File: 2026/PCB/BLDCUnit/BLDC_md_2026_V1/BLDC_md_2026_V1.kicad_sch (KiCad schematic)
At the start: 65 parts, among them J1 Conn_01x07_Pin, J2 Conn_01x02_Pin, J3 Conn_01x03_Socket, J4 Conn_01x02_Socket, J5 Conn_01x06_Socket, SW1 SW_MEC_5E, SW2 SW_MEC_5E, U1 MAX3051

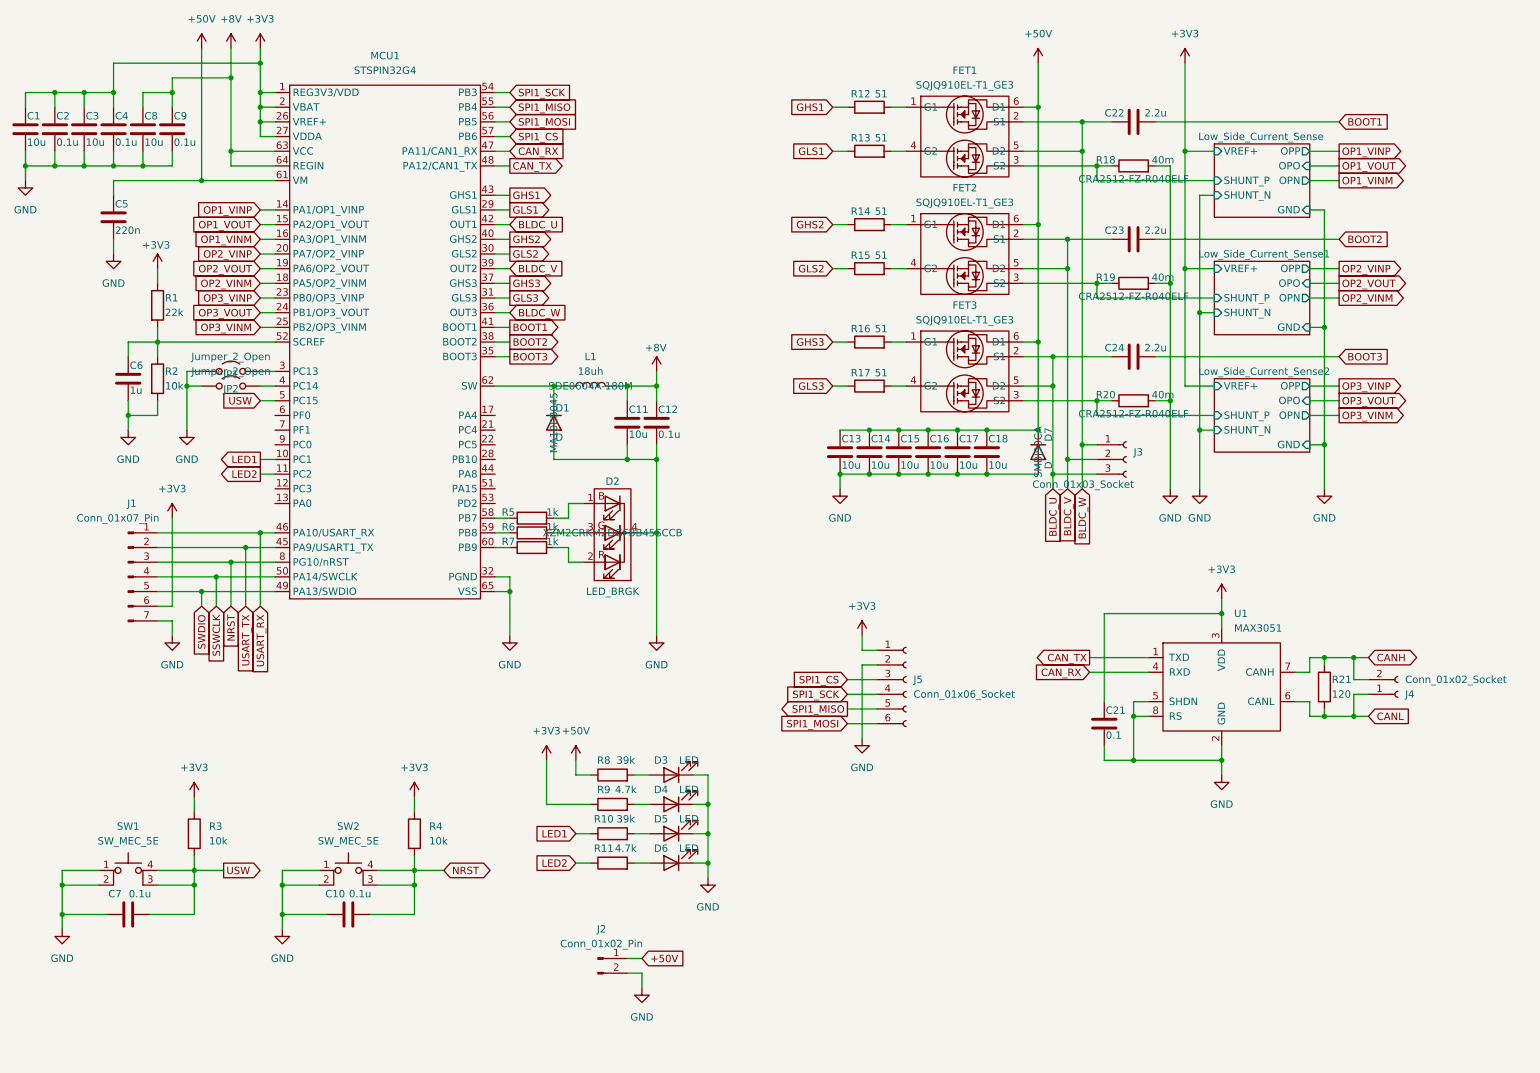
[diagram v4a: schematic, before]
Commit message: 外形縮小＆モエチャッカファイヤ回避
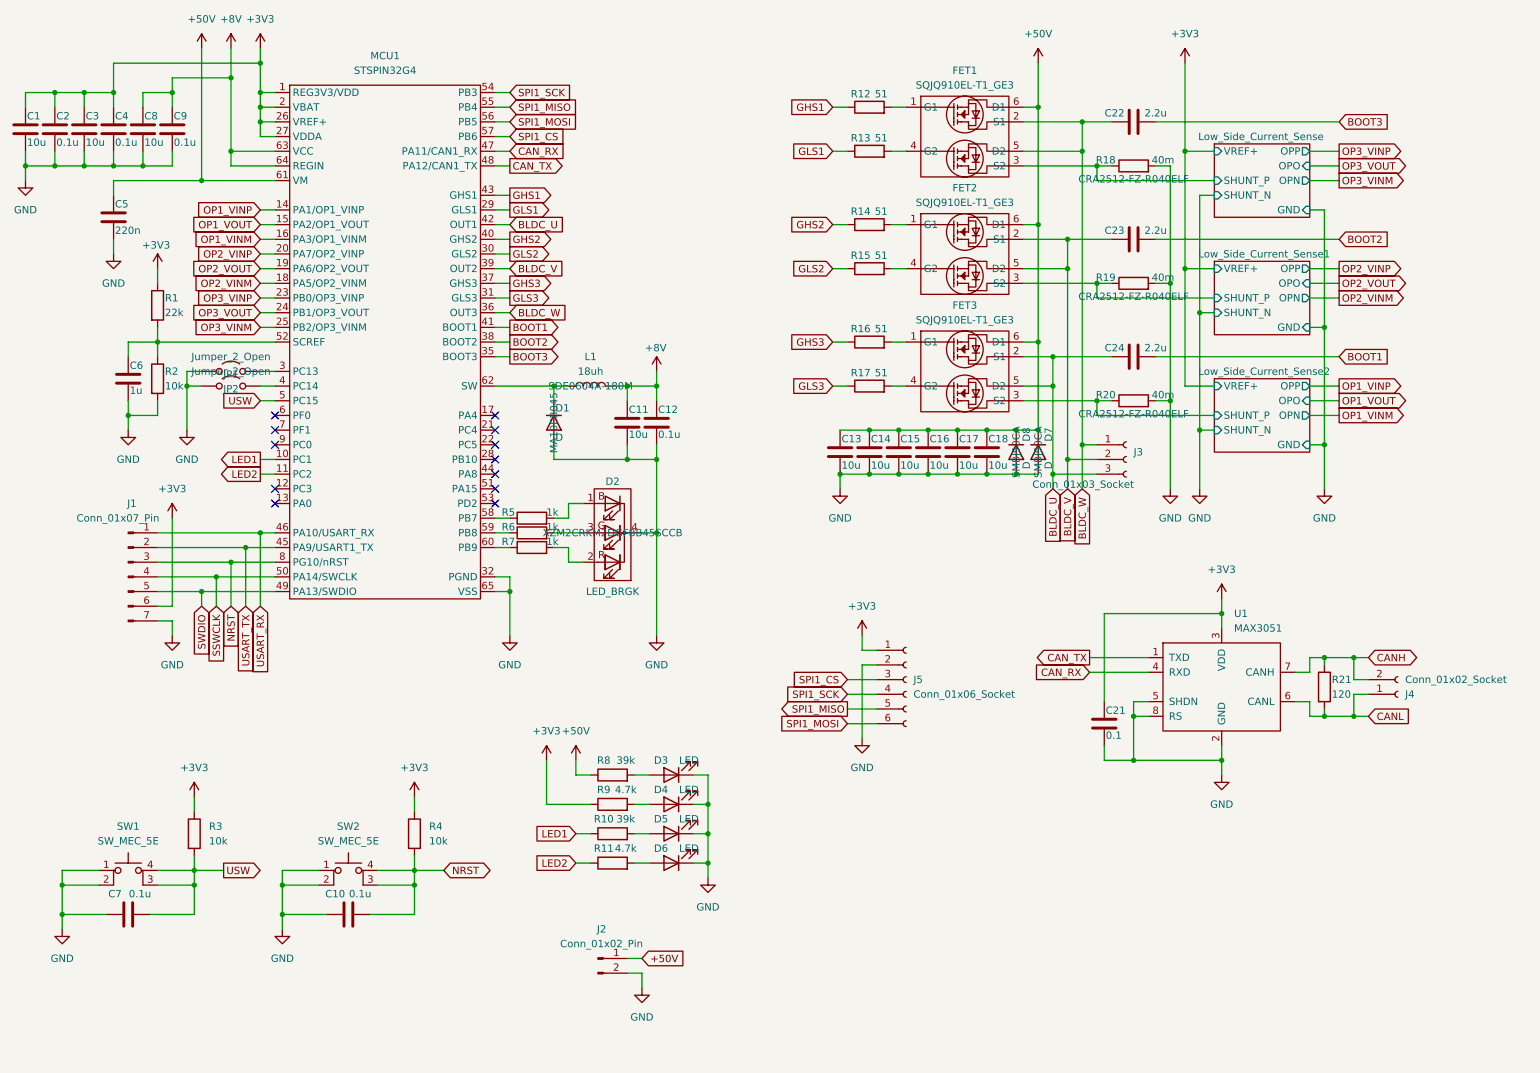
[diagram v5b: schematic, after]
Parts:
- added D8: D, Diode_SMD:D_SMB, symbol Device:D
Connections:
- net +50V: now also D8.1 (K)
- net BOOT1: now also C24.2; no longer C22.2
- net BOOT3: now also C22.2; no longer C24.2
- net GND: now also D8.2 (A)
- no-connect marks 0 -> 12
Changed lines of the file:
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@@
 	)
 	(junction
+		(at 194.31 87.63)
+		(diameter 0)
+		(color 0 0 0 0)
+	)
+	(junction
 		(at 229.87 119.38)
 		(diameter 0)
@@
 	)
 	(junction
+		(at 194.31 95.25)
+		(diameter 0)
+		(color 0 0 0 0)
+	)
+	(junction
 		(at 140.97 152.4)
 		(diameter 0)
@@
 		(color 0 0 0 0)
 	)
+	(no_connect
+		(at 104.14 92.71)
+	)
+	(no_connect
+		(at 66.04 87.63)
+	)
+	(no_connect
+		(at 66.04 100.33)
+	)
+	(no_connect
+		(at 104.14 97.79)
+	)
+	(no_connect
+		(at 104.14 100.33)
+	)
+	(no_connect
+		(at 104.14 87.63)
+	)
+	(no_connect
+		(at 66.04 90.17)
+	)
+	(no_connect
+		(at 104.14 90.17)
+	)
+	(no_connect
+		(at 104.14 85.09)
+	)
+	(no_connect
+		(at 104.14 95.25)
+	)
+	(no_connect
+		(at 66.04 97.79)
+	)
+	(no_connect
+		(at 66.04 85.09)
+	)
 	(wire
 		(pts
@@
 	(wire
 		(pts
-			(xy 189.23 95.25) (xy 198.12 95.25)
+			(xy 189.23 95.25) (xy 194.31 95.25)
 		)
 		(stroke
@@
 	(wire
 		(pts
-			(xy 189.23 87.63) (xy 198.12 87.63)
+			(xy 189.23 87.63) (xy 194.31 87.63)
 		)
 		(stroke
@@
 	(wire
 		(pts
+			(xy 194.31 95.25) (xy 198.12 95.25)
+		)
+		(stroke
+			(width 0)
+			(type default)
+		)
+	)
+	(wire
+		(pts
 			(xy 38.1 24.13) (xy 63.5 24.13)
 		)
@@
 	(wire
 		(pts
+			(xy 194.31 87.63) (xy 198.12 87.63)
+		)
+		(stroke
+			(width 0)
+			(type default)
+		)
+	)
+	(wire
+		(pts
 			(xy 140.97 157.48) (xy 140.97 162.56)
 		)
@@
 	(global_label "OP1_VINM"
 		(shape output)
-		(at 250.19 44.45 0)
+		(at 250.19 85.09 0)
 		(fields_autoplaced yes)
 		(effects
@@
 		)
 		(property "Intersheetrefs" "${INTERSHEET_REFS}"
-			(at 262.4281 44.45 0)
+			(at 262.4281 85.09 0)
 			(effects
 				(font
@@
 	(global_label "OP1_VINP"
 		(shape output)
-		(at 250.19 39.37 0)
+		(at 250.19 80.01 0)
 		(fields_autoplaced yes)
 		(effects
@@
 		)
 		(property "Intersheetrefs" "${INTERSHEET_REFS}"
-			(at 262.2467 39.37 0)
+			(at 262.2467 80.01 0)
 			(effects
 				(font
@@
 	(global_label "OP3_VINM"
 		(shape output)
-		(at 250.19 85.09 0)
+		(at 250.19 44.45 0)
 		(fields_autoplaced yes)
 		(effects
@@
 		)
 		(property "Intersheetrefs" "${INTERSHEET_REFS}"
-			(at 262.4281 85.09 0)
+			(at 262.4281 44.45 0)
 			(effects
 				(font
@@
 	(global_label "BOOT1"
 		(shape input)
-		(at 250.19 34.29 0)
+		(at 250.19 74.93 0)
 		(fields_autoplaced yes)
 		(effects
@@
 		)
 		(property "Intersheetrefs" "${INTERSHEET_REFS}"
-			(at 259.2833 34.29 0)
+			(at 259.2833 74.93 0)
 			(effects
 				(font
@@
 	(global_label "OP3_VOUT"
 		(shape output)
-		(at 250.19 82.55 0)
+		(at 250.19 41.91 0)
 		(fields_autoplaced yes)
 		(effects
@@
 		)
 		(property "Intersheetrefs" "${INTERSHEET_REFS}"
-			(at 262.67 82.55 0)
+			(at 262.67 41.91 0)
 			(effects
 				(font
@@
 	(global_label "OP3_VINP"
 		(shape output)
-		(at 250.19 80.01 0)
+		(at 250.19 39.37 0)
 		(fields_autoplaced yes)
 		(effects
@@
 		)
 		(property "Intersheetrefs" "${INTERSHEET_REFS}"
-			(at 262.2467 80.01 0)
+			(at 262.2467 39.37 0)
 			(effects
 				(font
@@
 	(global_label "BOOT3"
 		(shape input)
-		(at 250.19 74.93 0)
+		(at 250.19 34.29 0)
 		(fields_autoplaced yes)
 		(effects
@@
 		)
 		(property "Intersheetrefs" "${INTERSHEET_REFS}"
-			(at 259.2833 74.93 0)
+			(at 259.2833 34.29 0)
 			(effects
 				(font
@@
 	(global_label "OP1_VOUT"
 		(shape output)
-		(at 250.19 41.91 0)
+		(at 250.19 82.55 0)
 		(fields_autoplaced yes)
 		(effects
@@
 		)
 		(property "Intersheetrefs" "${INTERSHEET_REFS}"
-			(at 262.67 41.91 0)
+			(at 262.67 82.55 0)
 			(effects
 				(font
@@
 					(unit 1)
 				)
+			)
+		)
+	)
+	(symbol
+		(lib_id "Device:D")
+		(at 194.31 91.44 270)
+		(unit 1)
+		(exclude_from_sim no)
+		(in_bom yes)
+		(on_board yes)
+		(dnp no)
+		(property "Reference" "D8"
+			(at 196.088 88.392 0)
+			(effects
+				(font
+					(size 1.27 1.27)
+				)
+			)
+		)
+		(property "Value" "D"
+			(at 196.088 93.726 0)
+			(effects
+				(font
+					(size 1.27 1.27)
+				)
+			)
+		)
+		(property "Footprint" "Diode_SMD:D_SMB"
+			(at 194.31 91.44 0)
+			(effects
+				(font
+					(size 1.27 1.27)
+				)
+				(hide yes)
+			)
+		)
+		(property "Datasheet" "~"
+			(at 194.31 91.44 0)
+			(effects
+				(font
+					(size 1.27 1.27)
+				)
+				(hide yes)
+			)
+		)
+		(property "Description" "SMBJ90CA"
+			(at 194.31 91.44 0)
+			(effects
+				(font
+					(size 1.27 1.27)
+				)
+			)
+		)
+		(property "Sim.Device" "D"
+			(at 194.31 91.44 0)
+			(effects
+				(font
+					(size 1.27 1.27)
+				)
+				(hide yes)
+			)
+		)
+		(property "Sim.Pins" "1=K 2=A"
+			(at 194.31 91.44 0)
+			(effects
+				(font
+					(size 1.27 1.27)
+				)
+				(hide yes)
+			)
+		)
+		(pin "1"
+		)
+		(pin "2"
+		)
+		(instances
+			(project "BLDC_md_2026_V1"
+				(path "/b60d34e1-e978-4abb-befd-6af7b603dc53"
+					(reference "D8")
+					(unit 1)
+				)

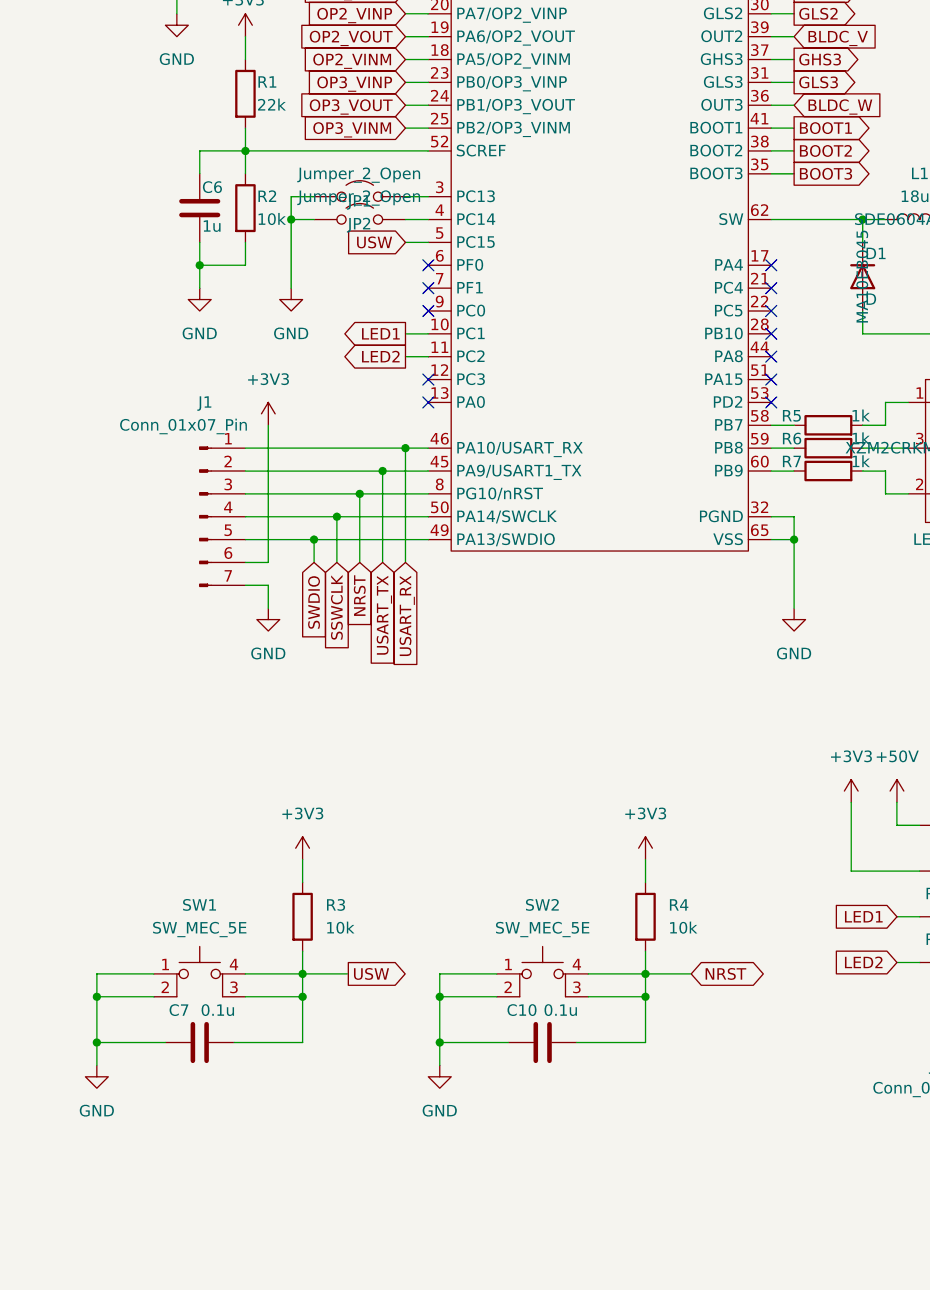
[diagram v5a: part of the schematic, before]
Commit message: 50V系統以外のコンデンサのサイズを1608から1005に変更 ＆MCU周りを配線
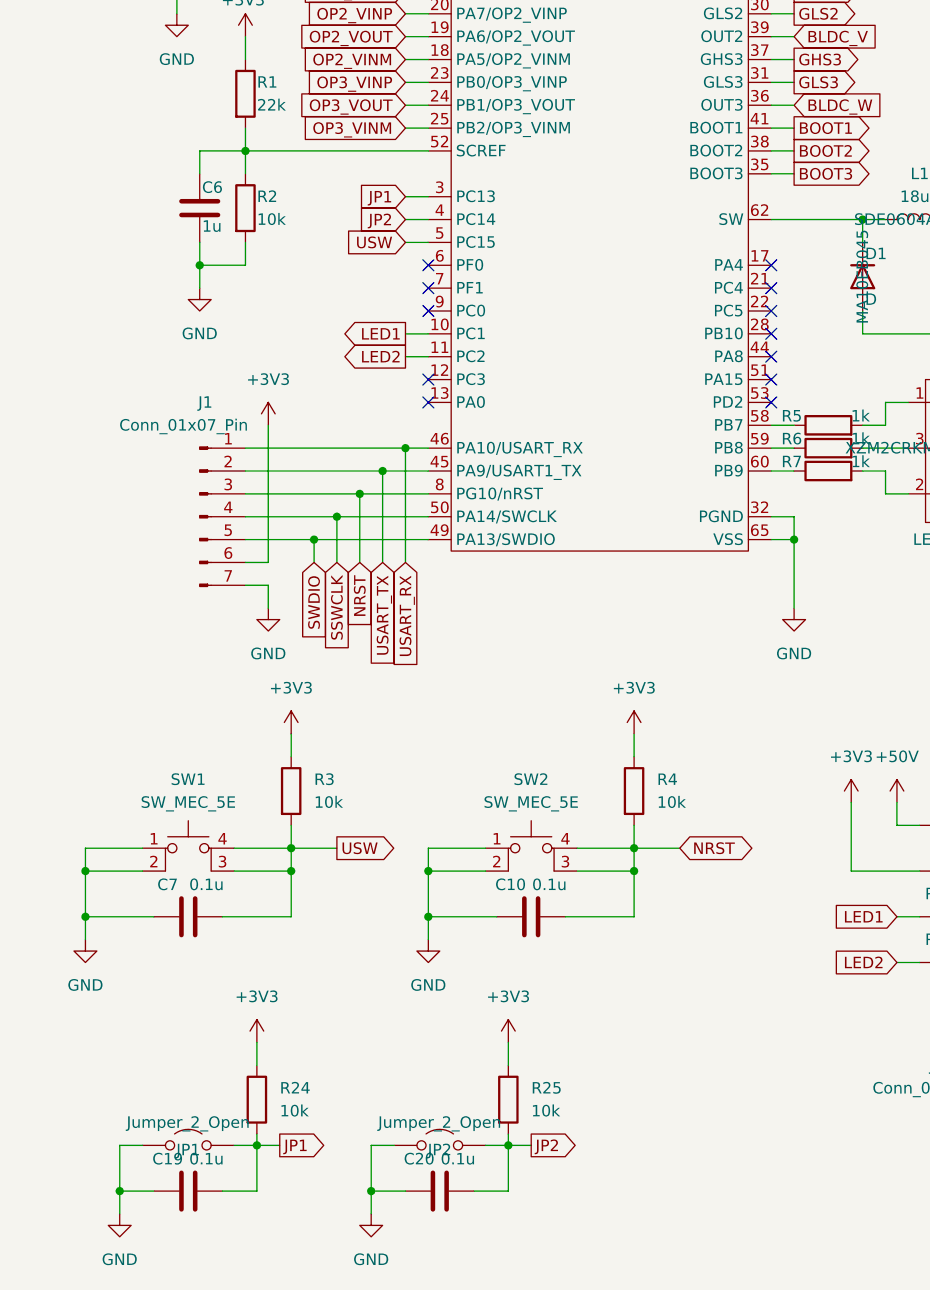
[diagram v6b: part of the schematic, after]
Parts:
- added C19, C20: 0.1u, Capacitor_SMD:C_0402_1005Metric_Pad0.74x0.62mm_HandSolder, symbol Device:C
- added R24, R25: 10k, Resistor_SMD:R_0402_1005Metric_Pad0.72x0.64mm_HandSolder, symbol Device:R
- C1, C2, C3, C4, C6: footprint Capacitor_SMD:C_0603_1608Metric_Pad1.08x0.95mm_HandSolder -> Capacitor_SMD:C_0402_1005Metric_Pad0.74x0.62mm_HandSolder
- R10, R11, R3, R4, R8, R9: footprint Resistor_SMD:R_0603_1608Metric_Pad0.98x0.95mm_HandSolder -> Resistor_SMD:R_0402_1005Metric_Pad0.72x0.64mm_HandSolder
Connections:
- net +3V3: now also R24.1, R25.1
- net GND: now also C19.2, C20.2
- net JP2: now reaches JP2.2 (B), MCU1.4 (PC14)
- net JP2: now also C20.1, R25.2
- net JP1: now reaches JP1.2 (B), MCU1.3 (PC13)
- net JP1: now also C19.1, R24.2
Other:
- moved on the sheet: C10, C7, JP1, JP2, R3, R4, SW1, SW2

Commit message: ビミョいのでUNDO
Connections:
- net GHS1: now also R16.1; no longer R12.1
- net GHS3: now also R12.1; no longer R16.1
- net GLS1: now also R17.1; no longer R13.1
- net GLS3: now also R13.1; no longer R17.1

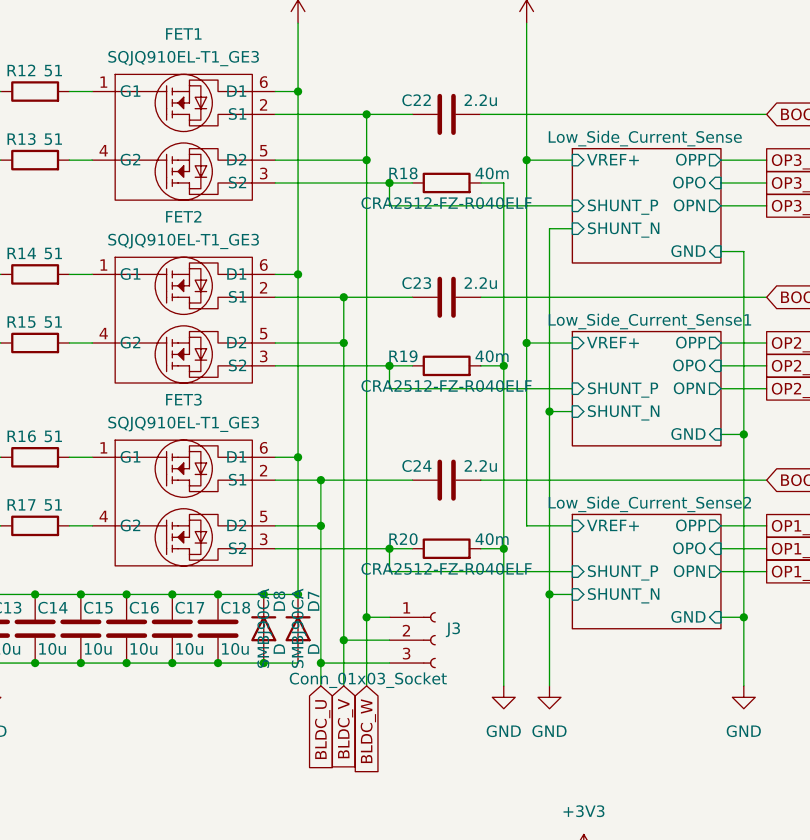
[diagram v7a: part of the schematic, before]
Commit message: シャント抵抗とTVSダイオードの型番変更
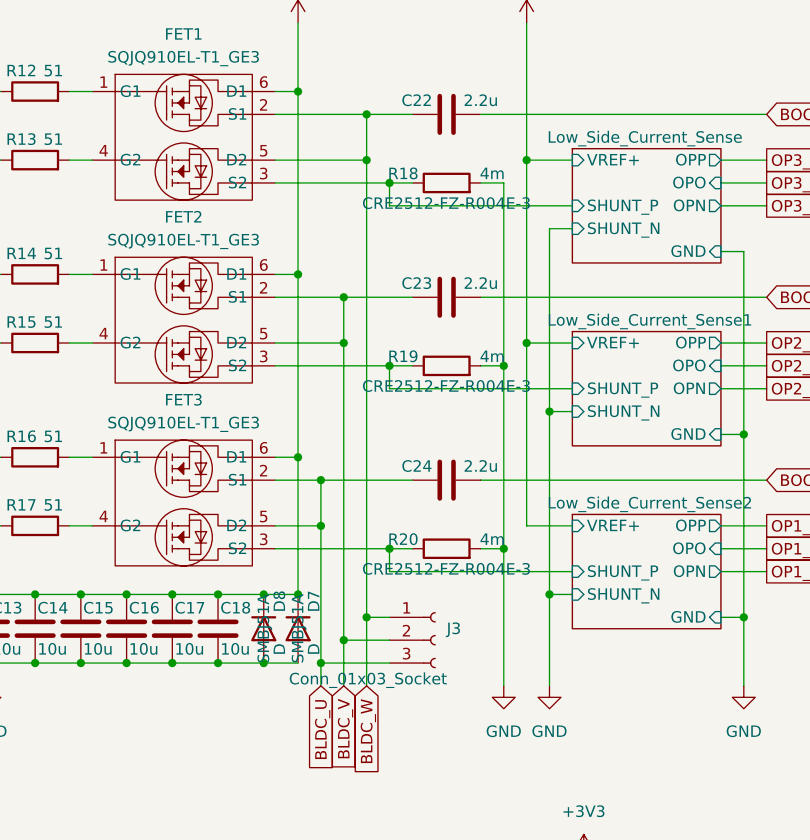
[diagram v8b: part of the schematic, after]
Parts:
- R18, R19, R20: value 40m -> 4m
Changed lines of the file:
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@@
 			)
 		)
-		(property "Description" "SMBJ90CA"
+		(property "Description" "SMBJ51A"
 			(at 194.31 91.44 0)
 			(effects
@@
 			)
 		)
-		(property "Value" "40m"
+		(property "Value" "4m"
 			(at 219.71 81.534 90)
 			(effects
@@
 			)
 		)
-		(property "Description" "CRA2512-FZ-R040ELF"
+		(property "Description" "CRE2512-FZ-R004E-3"
 			(at 214.63 84.836 90)
 			(effects
@@
 			)
 		)
-		(property "Value" "40m"
+		(property "Value" "4m"
 			(at 219.71 61.214 90)
 			(effects
@@
 			)
 		)
-		(property "Description" "CRA2512-FZ-R040ELF"
+		(property "Description" "CRE2512-FZ-R004E-3"
 			(at 214.63 64.516 90)
 			(effects
@@
 			)
 		)
-		(property "Value" "40m"
+		(property "Value" "4m"
 			(at 219.71 40.894 90)
 			(effects
@@
 			)
 		)
-		(property "Description" "CRA2512-FZ-R040ELF"
+		(property "Description" "CRE2512-FZ-R004E-3"
 			(at 214.63 44.196 90)
 			(effects
@@
 			)
 		)
-		(property "Description" "SMBJ90CA"
+		(property "Description" "SMBJ51A"
 			(at 198.12 91.44 0)
 			(effects
